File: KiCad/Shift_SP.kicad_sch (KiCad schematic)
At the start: 37 parts, among them J101 2mm_clamp, J102 2mm_clamp, J103 2mm_clamp, J104 2mm_clamp, J105 2mm_clamp, J106 2mm_clamp, J107 2mm_clamp, J108 2mm_clamp, J109 2mm_clamp, J110 2mm_clamp, J111 2mm_clamp, J112 2mm_clamp, J113 2mm_clamp, J114 2mm_clamp, J115 2mm_clamp, J116 2mm_clamp, J117 2mm_clamp, J118 2mm_clamp, J119 2mm_clamp, J120 2mm_clamp, J121 2mm_clamp, J122 2mm_clamp, J123 2mm_clamp, J124 2mm_clamp, J125 2mm_clamp, J126 2mm_clamp, J127 2mm_clamp, J128 2mm_clamp, J129 2mm_clamp, U136 74HC595D,118, U137 74HC595D,118, U138 74HC595D,118, U139 74HC595D,118

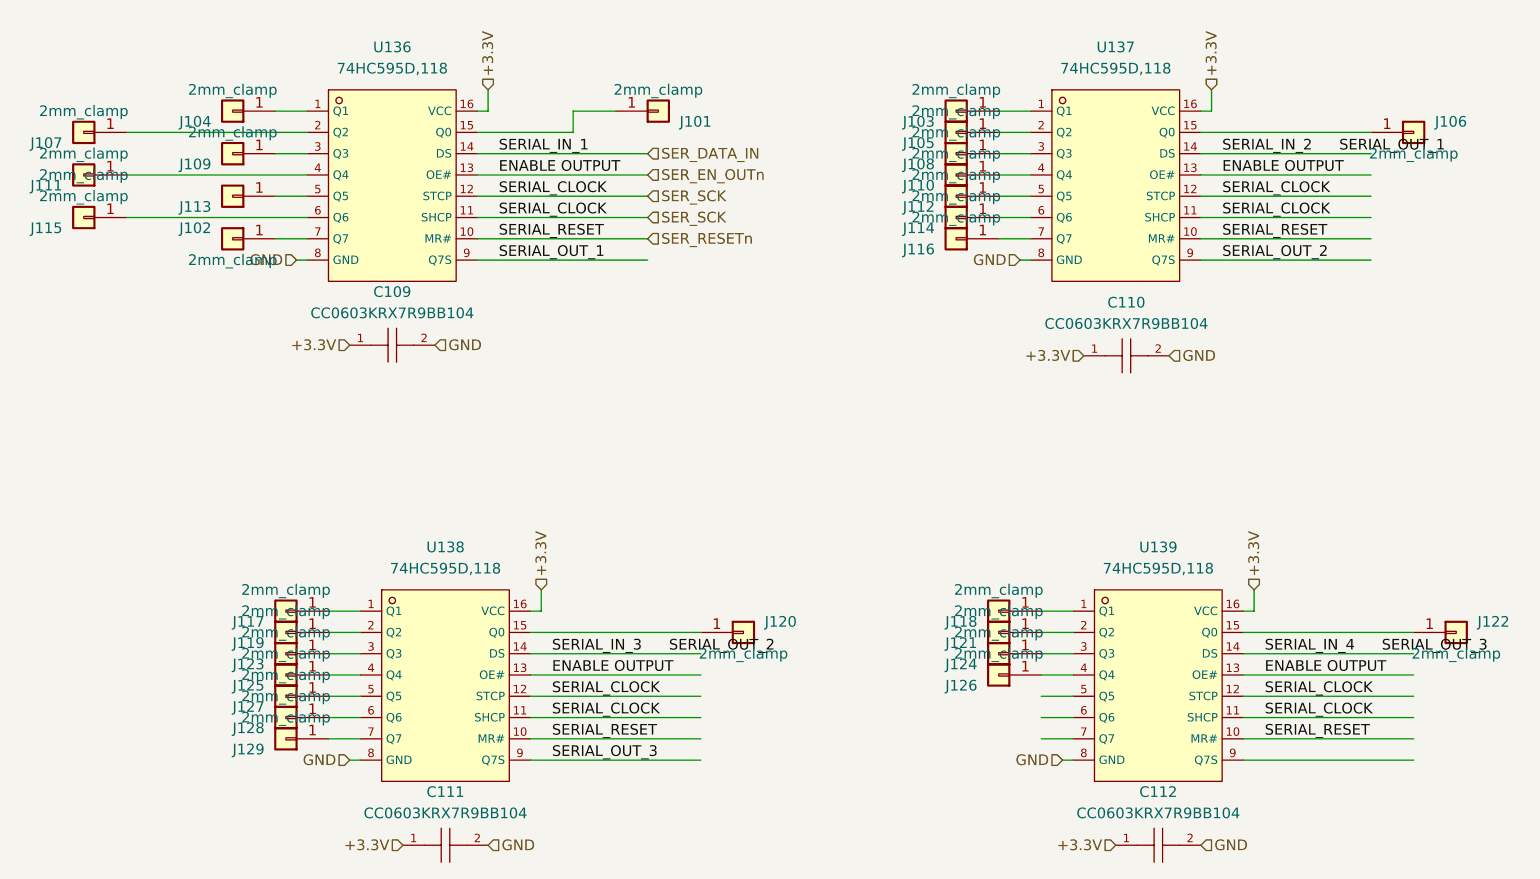
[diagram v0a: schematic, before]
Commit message: Ready for PCB layout with discreet LEDs
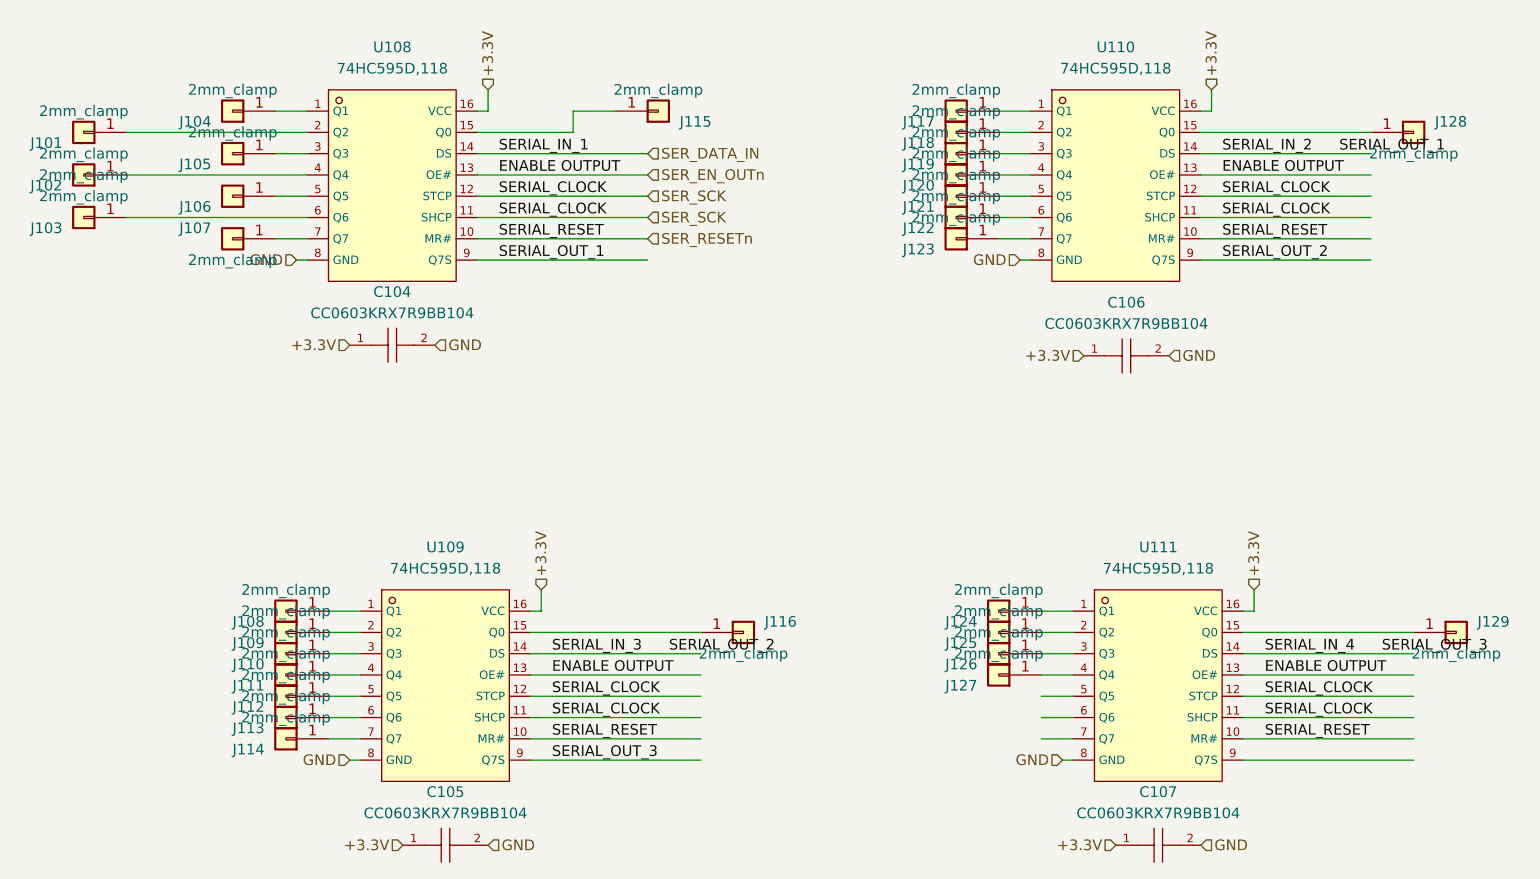
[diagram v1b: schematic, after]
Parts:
- renumbered C109 to C104, C111 to C105, C110 to C106, C112 to C107, J107 to J101, J111 to J102, J115 to J103, J109 to J105, J113 to J106, J102 to J107, J117 to J108, J119 to J109, J123 to J110, J125 to J111, J127 to J112, J128 to J113, J129 to J114, J101 to J115, J120 to J116, J103 to J117, J105 to J118, J108 to J119, J110 to J120, J112 to J121, J114 to J122, J116 to J123, J118 to J124, J121 to J125, J124 to J126, J126 to J127, J106 to J128, J122 to J129, U136 to U108, U138 to U109, U137 to U110, U139 to U111
